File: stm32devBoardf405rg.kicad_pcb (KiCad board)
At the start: 4 copper layers, 54 parts, among them J1 Screw_Terminal_01x02, J2 SWD, J3 Conn_01x04, J4 Conn_01x04, J5 USB_B_Micro, Q1 AO3401A, SW1 SW_SPDT, U1 STM32F405RGT6, U2 USBLC6-2SC6, Y1 16MZ

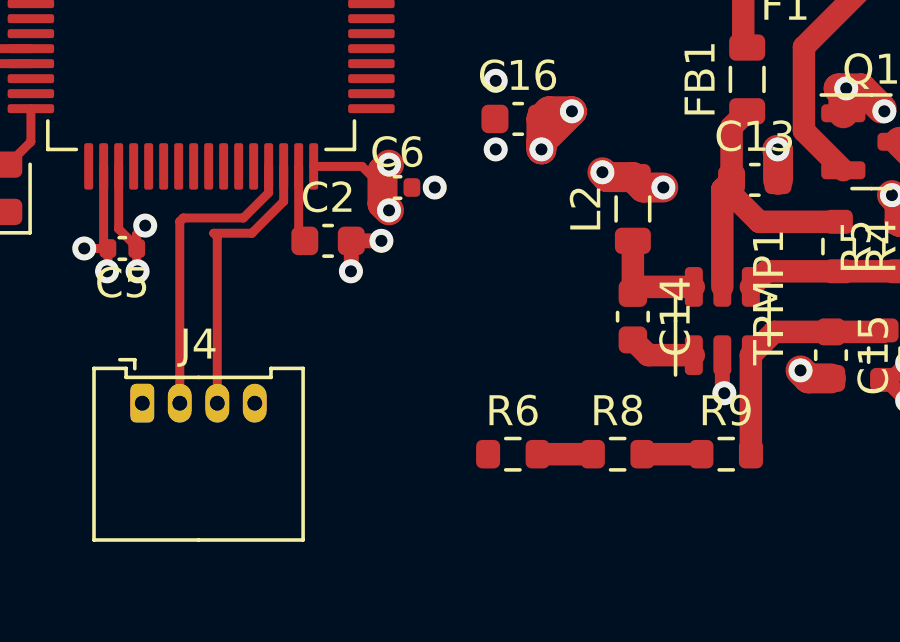
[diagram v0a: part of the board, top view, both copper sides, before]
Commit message: fixed via routing issue
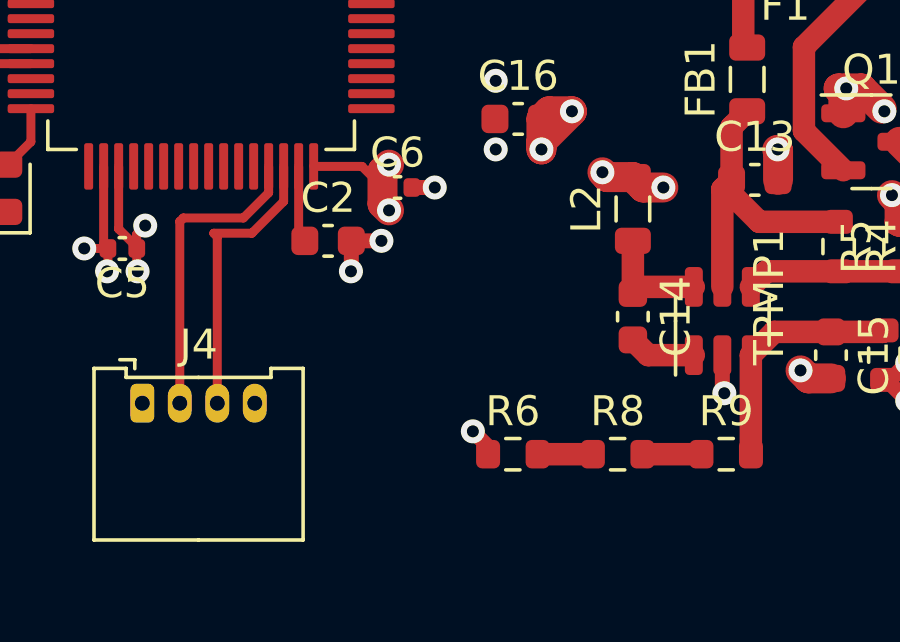
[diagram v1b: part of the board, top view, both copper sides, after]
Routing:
- net +3.3V: track 44.7 -> 45.7 mm, vias 21 -> 22
- net GND: track 58.1 -> 58.9 mm
- added copper zone on In2.Cu, net GND
- removed copper zone on In2.Cu, net +3.3V
- removed copper zone on In1.Cu, net GND
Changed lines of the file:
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@@
   (segment (start 117.348 136.906) (end 117.856 136.906) (width 1) (layer "F.Cu") (net 2))
   (segment (start 104.14 128.016) (end 104.14 129.006) (width 0.5) (layer "F.Cu") (net 2))
+  (segment (start 103.632 140.208) (end 102.87 140.208) (width 0.5) (layer "F.Cu") (net 2))
   (segment (start 123.444 124.206) (end 124.46 124.206) (width 0.5) (layer "F.Cu") (net 2))
   (segment (start 100.851 141.986) (end 100.851 142.989) (width 0.5) (layer "F.Cu") (net 2))
@@
   (segment (start 93.698 142.193154) (end 93.698 142.24) (width 0.3) (layer "F.Cu") (net 4))
   (segment (start 92.095 125.087) (end 91.976 124.968) (width 0.25) (layer "F.Cu") (net 4))
+  (segment (start 105.41 149.098) (end 105.41 148.844) (width 0.5) (layer "F.Cu") (net 4))
   (segment (start 102.58 128.742) (end 102.108 128.742) (width 1) (layer "F.Cu") (net 4))
   (segment (start 87.464 130.08) (end 87.376 129.992) (width 0.25) (layer "F.Cu") (net 4))
@@
   (segment (start 101.89 139.664) (end 102.108 139.446) (width 1) (layer "F.Cu") (net 4))
   (segment (start 107.652 112.732) (end 107.188 112.268) (width 1) (layer "F.Cu") (net 4))
+  (segment (start 105.41 148.844) (end 104.902 148.336) (width 0.5) (layer "F.Cu") (net 4))
   (segment (start 101.207 139.505) (end 101.91 140.208) (width 0.3) (layer "F.Cu") (net 4))
   (segment (start 111.252 140.208) (end 110.583 140.208) (width 1) (layer "F.Cu") (net 4))
@@
   (segment (start 109.791 126.555) (end 109.728 126.492) (width 1) (layer "F.Cu") (net 4))
   (via (at 115.824 146.304) (size 0.8) (drill 0.4) (layers "F.Cu" "B.Cu") (free) (net 4))
+  (via (at 104.902 148.336) (size 0.8) (drill 0.4) (layers "F.Cu" "B.Cu") (free) (net 4))
   (via (at 108.204 137.668) (size 0.8) (drill 0.4) (layers "F.Cu" "B.Cu") (free) (net 4))
   (via (at 93.726 143.002) (size 0.8) (drill 0.4) (layers "F.Cu" "B.Cu") (free) (net 4))
@@
   (segment (start 101.52 131.58) (end 102.682501 131.58) (width 0.261112) (layer "F.Cu") (net 74))
   (segment (start 109.119836 131.597844) (end 114.711836 126.005844) (width 0.261112) (layer "F.Cu") (net 74))
-  (zone (net 2) (net_name "GND") (layer "In1.Cu") (hatch edge 0.5)
+  (zone (net 4) (net_name "+3.3V") (layer "In1.Cu") (hatch edge 0.5)
+    (priority 1)
     (connect_pads (clearance 0.5))
     (min_thickness 0.25) (filled_areas_thickness no)
@@
     (polygon
       (pts
-        (xy 68.58 107.188)
-        (xy 133.604 107.696)
-        (xy 133.35 159.766)
-        (xy 68.072 159.004)
+        (xy 68.58 108.966)
+        (xy 133.858 108.966)
+        (xy 133.35 160.02)
+        (xy 68.834 157.226)
       )
     )
   )
-  (zone (net 4) (net_name "+3.3V") (layers "In1.Cu" "In2.Cu") (hatch edge 0.5)
+  (zone (net 2) (net_name "GND") (layer "In2.Cu") (hatch edge 0.5)
     (connect_pads (clearance 0.5))
     (min_thickness 0.25) (filled_areas_thickness no)
@@
       (pts
         (xy 68.58 107.3069)
-        (xy 133.604 107.8149)
+        (xy 133.35 107.95)
         (xy 133.35 159.8849)
         (xy 68.072 159.1229)

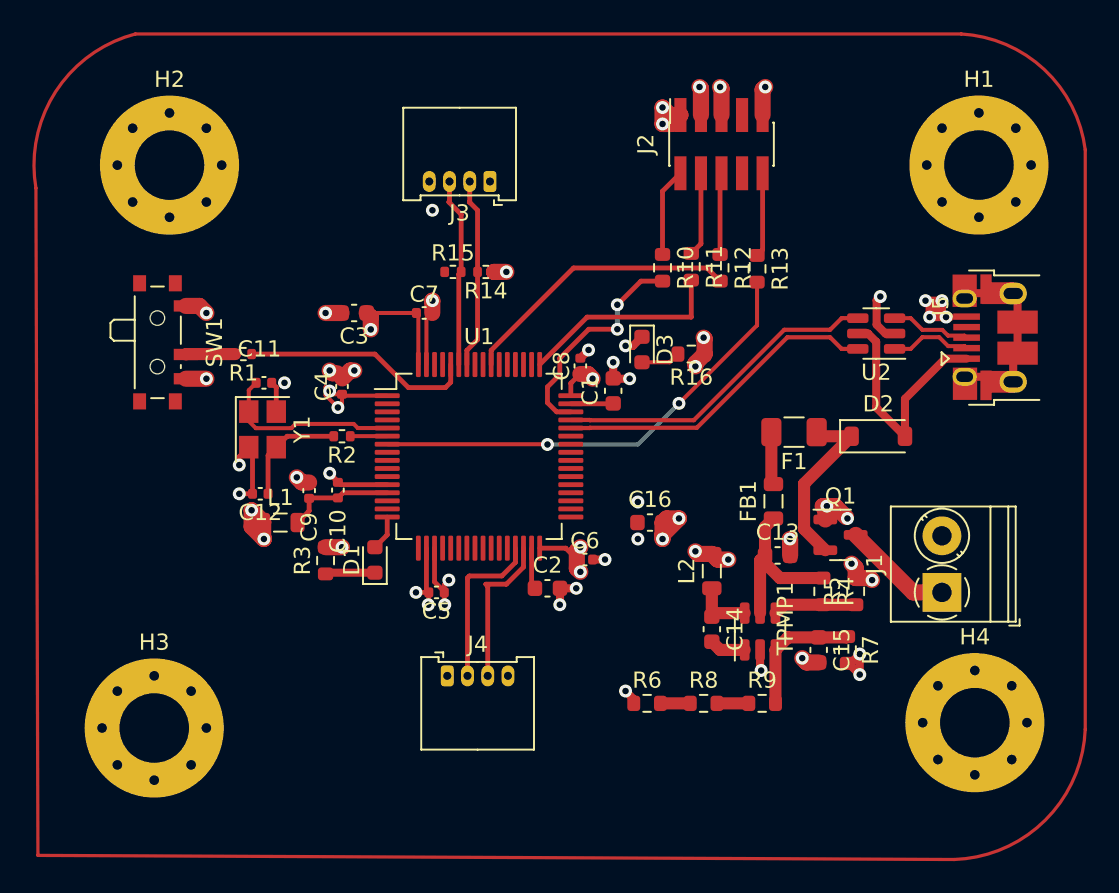
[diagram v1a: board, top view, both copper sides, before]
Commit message: corrected fill layers and added edge cuts
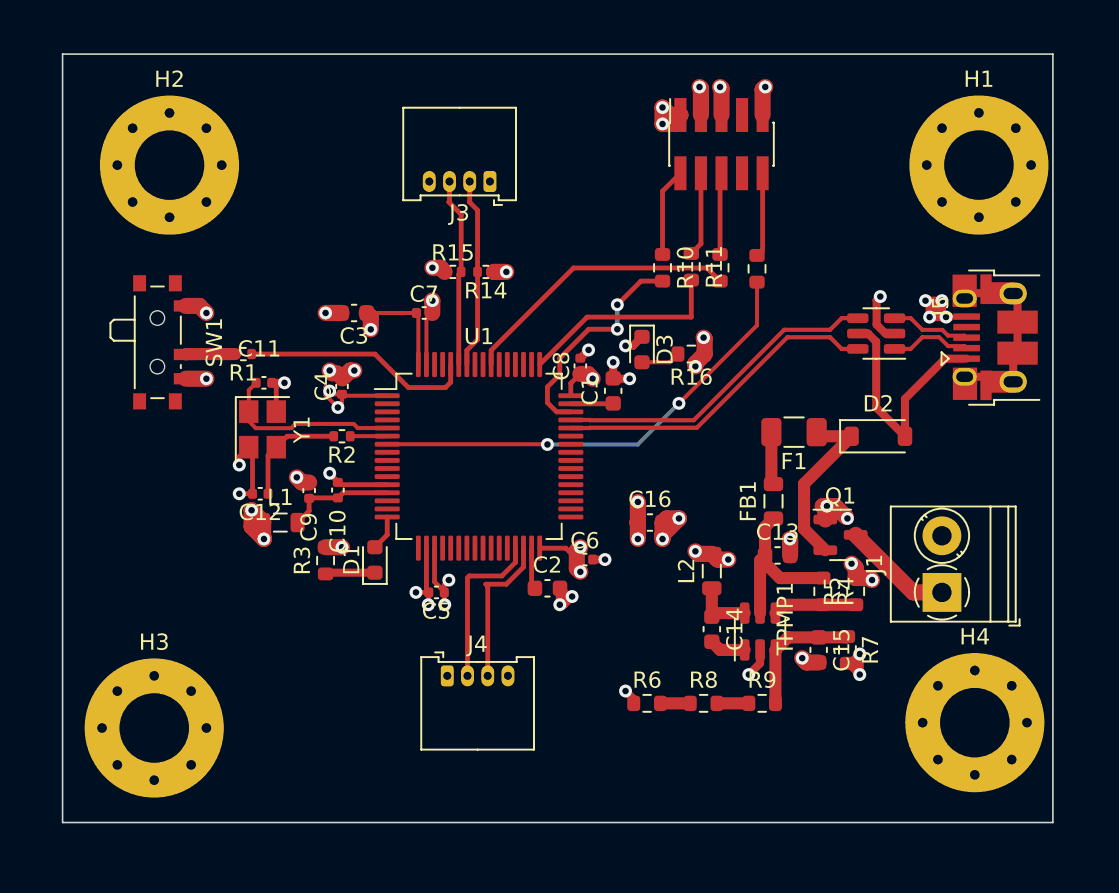
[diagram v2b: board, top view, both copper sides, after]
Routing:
- net GND: track 58.9 -> 63.4 mm, vias 39 -> 38
- net +3.3V: track 45.7 -> 46.5 mm, vias 22 -> 23
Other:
- board outline added: 61.2 x 47.5 mm

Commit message: removed unnecssary values and reference from silkscreen
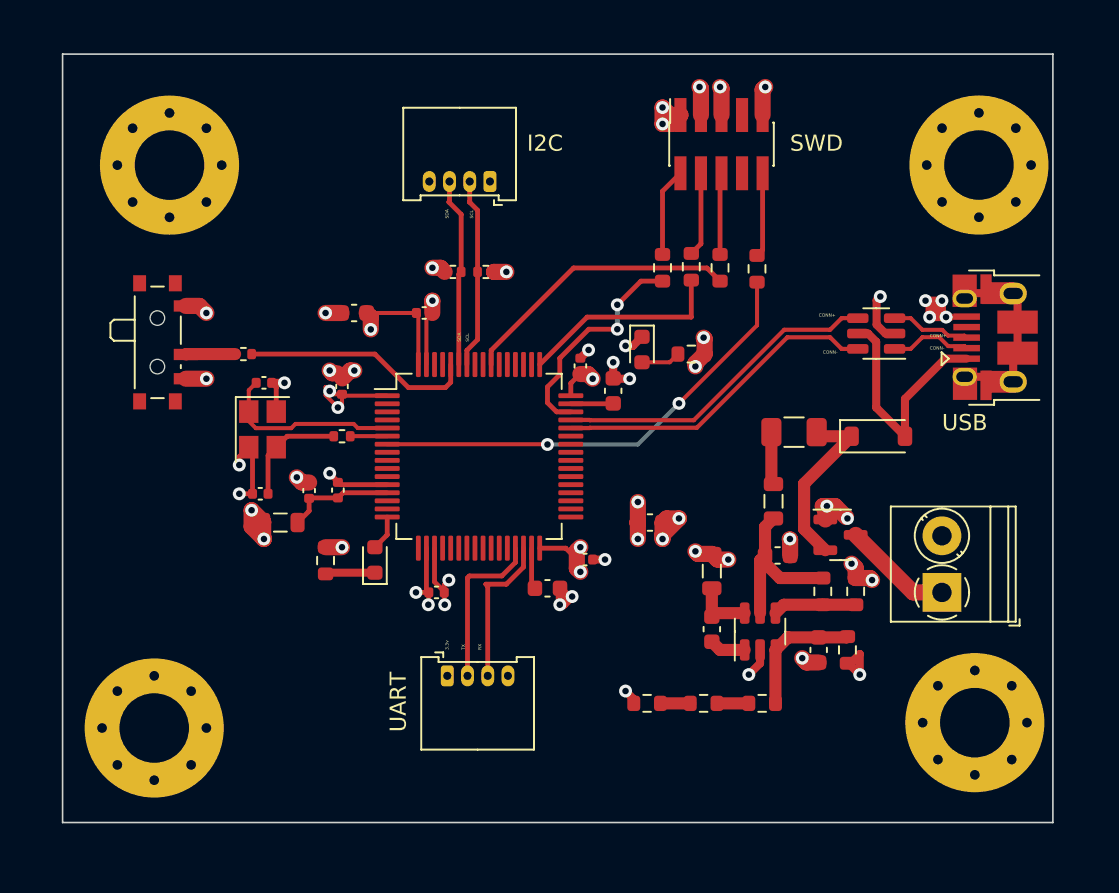
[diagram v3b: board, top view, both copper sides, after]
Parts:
- renumbered J3 to I2C
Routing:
- net GND: vias 38 -> 37
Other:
- board text added: "3.3v"
- board text added: "CONN+"
- board text added: "CONN-"
- board text added: "I2C"
- board text added: "RX"
- board text added: "SCL"
- board text added: "SDA"
- board text added: "SWD"
- board text added: "TX"
- board text added: "UART"
- board text added: "USB"

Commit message: replaced swd footprint
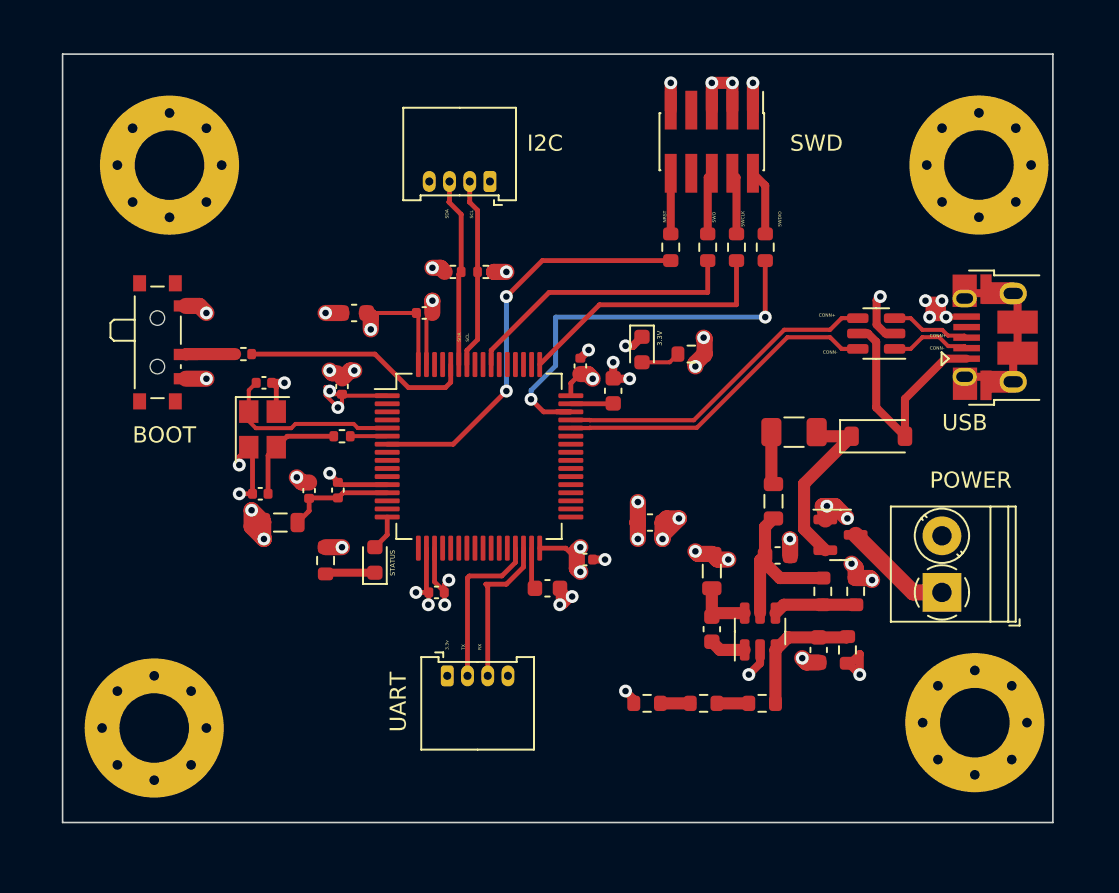
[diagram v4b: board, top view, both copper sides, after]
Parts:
- J2: footprint Connector_PinSocket_1.27mm:PinSocket_2x05_P1.27mm_Vertical_SMD -> Connector_PinHeader_1.27mm:PinHeader_2x05_P1.27mm_Vertical_SMD
- moved R10 6.48 mm to (113.5, 120.9)
- moved R13 5.50 mm to (107.7, 120.9)
- moved R11 3.04 mm to (111.8, 120.9)
- moved R12 1.48 mm to (110.0, 120.9)
- moved J2 0.62 mm to (110.2, 114.4), turned to -90 degrees
- renumbered I2C to J3
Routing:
- net SWDIO: track 14.0 -> 25.8 mm
- net SWCLK: track 12.9 -> 16.4 mm
- net NRST: track 28.6 -> 25.6 mm
- net +3.3V: track 46.5 -> 44.6 mm, vias 23 -> 22
- net Net-(J2-Pin_10): track 5.22 -> 3.75 mm
- net Net-(J2-Pin_2): track 5.48 -> 4.06 mm
- net Net-(J2-Pin_4): track 5.20 -> 3.85 mm
- net Net-(J2-Pin_6): track 5.05 -> 3.85 mm
- net GND: track 63.4 -> 64.4 mm
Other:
- board text added: "3.3V"
- board text added: "BOOT"
- board text added: "NRST"
- board text added: "POWER"
- board text added: "STATUS"
- board text added: "SWCLK"
- board text added: "SWDIO"
- board text added: "SWO"

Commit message: first STM32 board,final commit
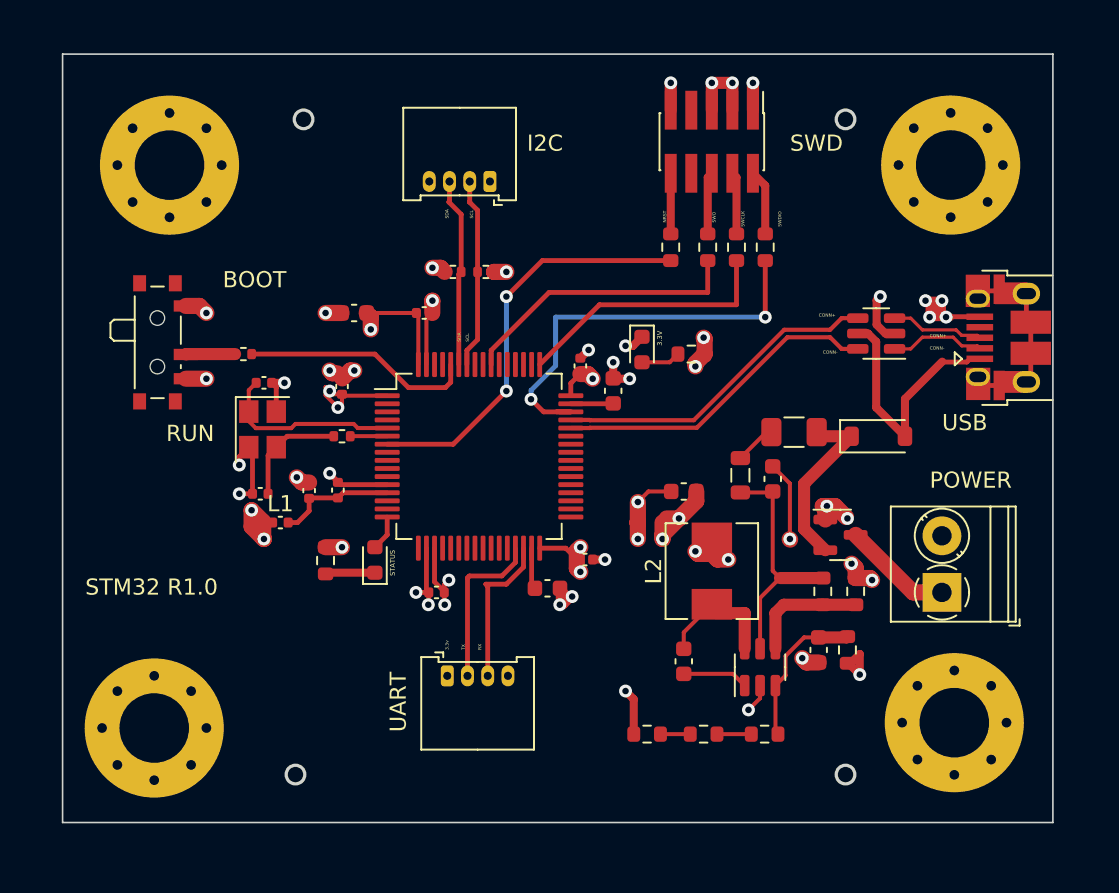
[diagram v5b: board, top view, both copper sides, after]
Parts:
- L1: value 3u3 -> 39n; footprint Inductor_SMD:L_0805_2012Metric -> Capacitor_SMD:C_0402_1005Metric
- L2: value 3u3 -> 10uH; footprint Inductor_SMD:L_0805_2012Metric -> Inductor_SMD:L_Sunlord_MWSA0503S
- moved C13 4.74 mm to (114.0, 135.2), turned to 90 degrees
- moved C16 2.84 mm to (108.5, 136.0)
- moved C14 2.64 mm to (108.5, 146.5)
- moved FB1 2.60 mm to (112.0, 135.0)
- moved TPMP2359DJ1 2.20 mm to (113.2, 146.9)
- moved R9 1.91 mm to (113.5, 151.0)
- moved R6 1.90 mm to (106.2, 151.0)
- moved R8 1.90 mm to (109.7, 151.0)
- moved H1 1.75 mm to (125.0, 115.8)
- moved H4 1.27 mm to (125.2, 150.3)
- moved J5 0.82 mm to (128.6, 126.5)
- renumbered TPMP1 to TPMP2359DJ1
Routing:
- net GND: track 64.4 -> 72.8 mm
- net BUCK_IN: track 10.6 -> 15.1 mm
- net +3.3V: track 44.6 -> 48.2 mm
- net BUCK_SW: track 3.87 -> 7.49 mm
- net unconnected-(J5-Shield-Pad6)_3: track 10.9 -> 8.39 mm
- net BUCK_EN: track 5.17 -> 7.38 mm
- net BUCK_BS: track 2.24 -> 4.07 mm
- net BUCK_FB: track 8.10 -> 9.48 mm
- net +5V: track 15.1 -> 15.9 mm
- net USB_CONN_D-: track 5.03 -> 5.85 mm
- net USB_CONN_D+: track 4.95 -> 5.77 mm
- net Net-(F1-Pad2): track 3.26 -> 2.58 mm
- net +3.3VA: track 6.76 -> 7.34 mm
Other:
- outline, holes or cut-outs redrawn
- board text added: "RUN"
- board text added: "STM32 R1.0"
